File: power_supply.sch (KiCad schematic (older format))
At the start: 0 parts

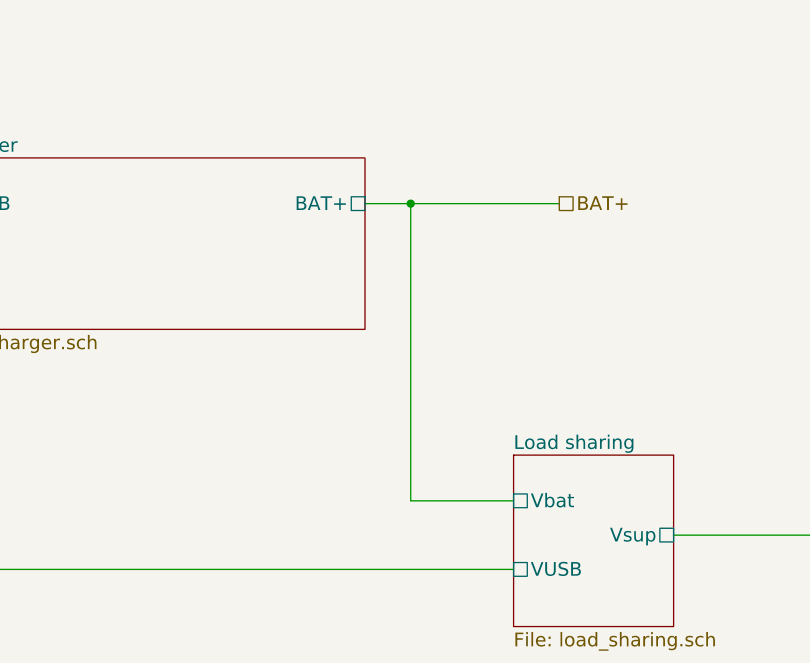
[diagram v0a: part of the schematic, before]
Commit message: Fixed NTLJF3117P MOSFET pin layout
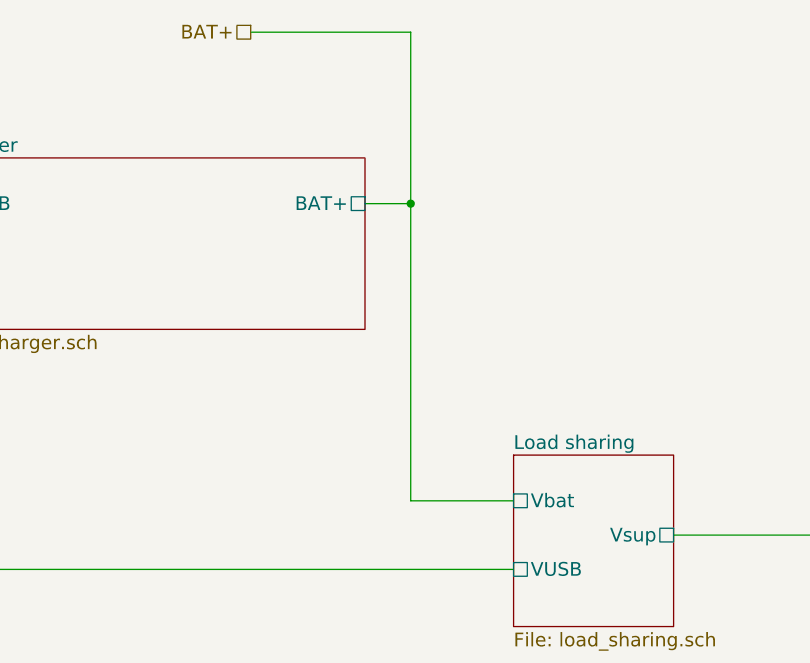
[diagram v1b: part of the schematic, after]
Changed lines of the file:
@@
 Text HLabel 1400 2900 0    60   UnSpc ~ 0
 VUSB
-Text HLabel 4800 2900 2    60   UnSpc ~ 0
+Text HLabel 3450 2150 0    60   UnSpc ~ 0
 BAT+
 $Sheet
@@
 $EndSheet
 Wire Wire Line
-	3950 2900 4800 2900
+	3950 2900 4150 2900
+Wire Wire Line
+	4150 2150 4150 4200
 Wire Wire Line
 	1400 2900 2100 2900
-Wire Wire Line
-	4150 2900 4150 4200
 Wire Wire Line
 	4150 4200 4600 4200
@@
 Wire Wire Line
 	8450 4400 7900 4400
+Wire Wire Line
+	3450 2150 4150 2150
 $EndSCHEMATC

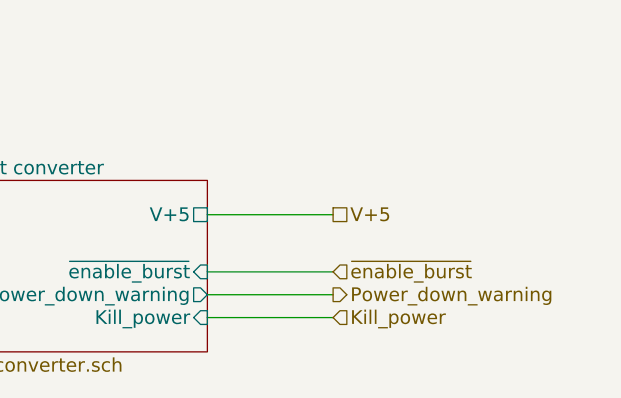
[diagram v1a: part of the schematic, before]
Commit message: Moved MCU pins around to make sure that they do not interfere with the programmer Moved ISP Header closer to the edge of the board to allow easier access with the programmer Added pulldown resistor to the DCD/DC converters enable pin to make sure it stays off in case of failure Added more PDFs of components
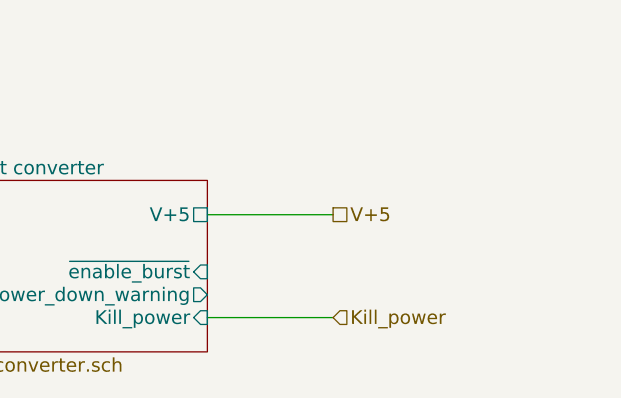
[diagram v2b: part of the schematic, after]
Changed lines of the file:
@@
 Wire Wire Line
 	8450 4600 7900 4600
-Text HLabel 8450 4500 2    60   Output ~ 0
-Power_down_warning
-Wire Wire Line
-	8450 4500 7900 4500
-Text HLabel 8450 4400 2    60   Input ~ 0
-~enable_burst
-Wire Wire Line
-	8450 4400 7900 4400
 Wire Wire Line
 	3450 2150 4150 2150

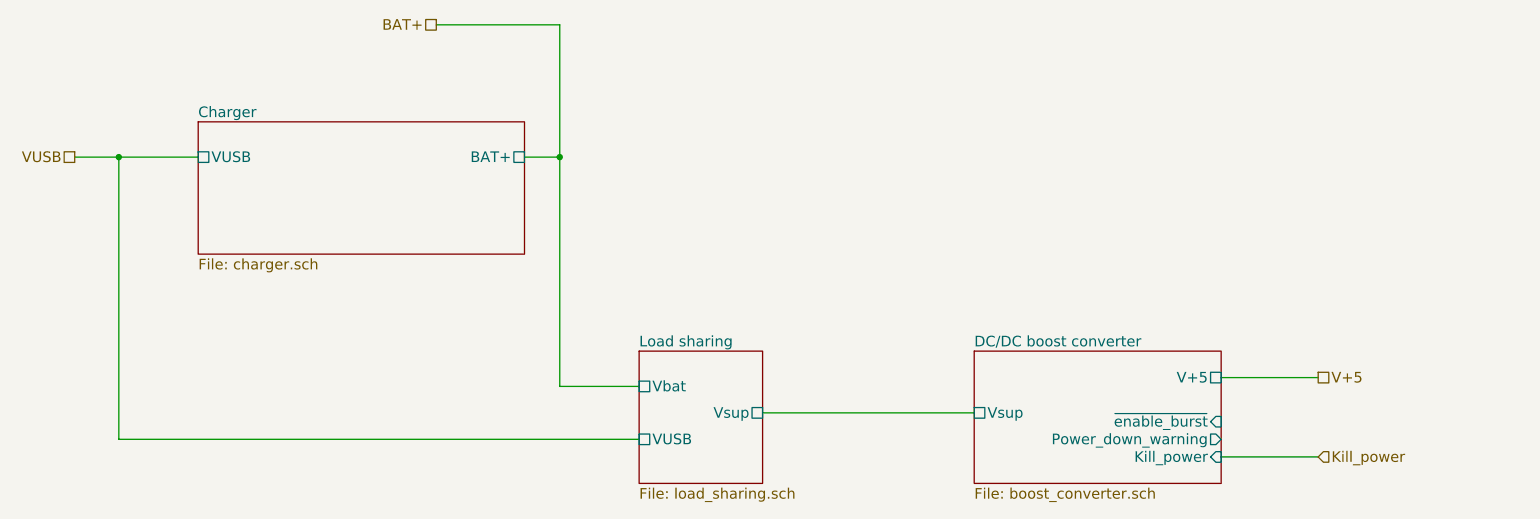
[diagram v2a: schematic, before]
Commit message: Preparing for v1.2 Updated to KiCAD 5 nightly Added resistors to isolate the programming pins Added transistor to drive the LED Replaced LTC3458 boost converter with an LTC3536 buck-boost converter to step down the USB power supply Added debugging jumper to test the voltage regulator
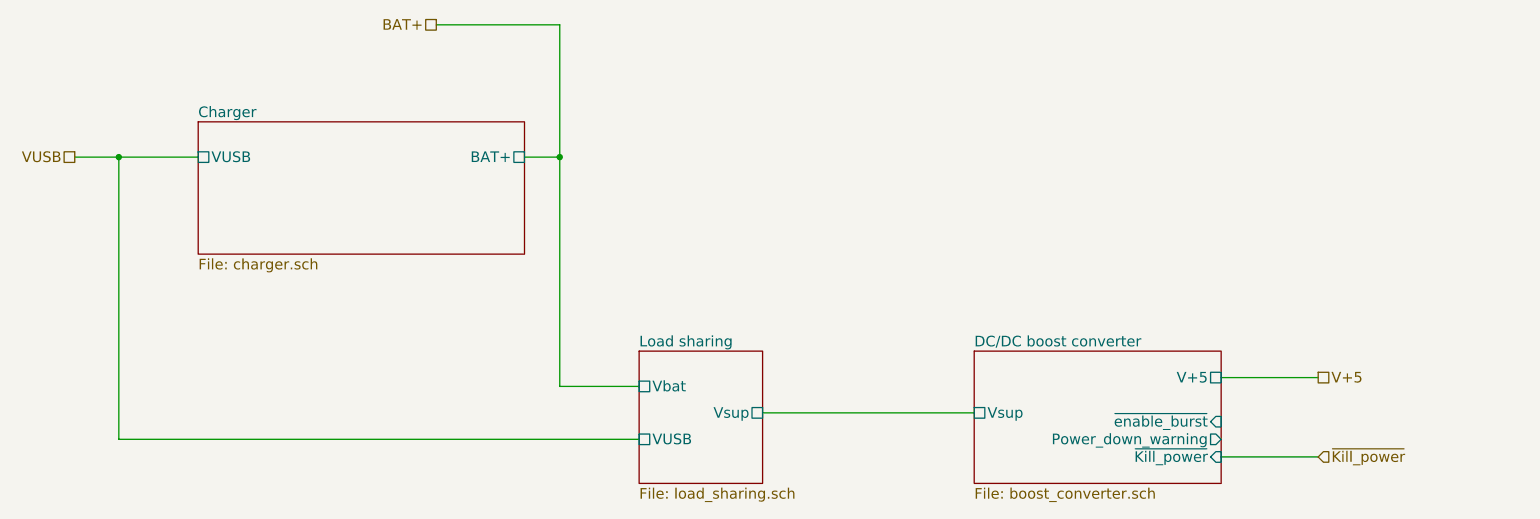
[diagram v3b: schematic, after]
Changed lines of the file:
@@
-EESchema Schematic File Version 2
-LIBS:power
-LIBS:device
-LIBS:transistors
-LIBS:conn
-LIBS:linear
-LIBS:regul
-LIBS:74xx
-LIBS:cmos4000
-LIBS:adc-dac
-LIBS:memory
-LIBS:xilinx
-LIBS:microcontrollers
-LIBS:dsp
-LIBS:microchip
-LIBS:analog_switches
-LIBS:motorola
-LIBS:texas
-LIBS:intel
-LIBS:audio
-LIBS:interface
-LIBS:digital-audio
-LIBS:philips
-LIBS:display
-LIBS:cypress
-LIBS:siliconi
-LIBS:opto
-LIBS:atmel
-LIBS:contrib
-LIBS:valves
-LIBS:switches
-LIBS:Microchip
-LIBS:On Semiconductor
-LIBS:Linear Technology
+EESchema Schematic File Version 4
 LIBS:main-cache
 EELAYER 26 0
@@
 	3950 2900 4150 2900
 Wire Wire Line
-	4150 2150 4150 4200
+	4150 2150 4150 2900
 Wire Wire Line
-	1400 2900 2100 2900
+	1400 2900 1650 2900
 Wire Wire Line
 	4150 4200 4600 4200
@@
 F3 "V+5" U R 7900 4150 60
 F4 "Power_down_warning" O R 7900 4500 60
-F5 "Kill_power" I R 7900 4600 60
+F5 "~Kill_power" I R 7900 4600 60
 F6 "~enable_burst" I R 7900 4400 60
 $EndSheet
@@
 	7900 4150 8450 4150
 Text HLabel 8450 4600 2    60   Input ~ 0
-Kill_power
+~Kill_power
 Wire Wire Line
 	8450 4600 7900 4600
 Wire Wire Line
 	3450 2150 4150 2150
+Wire Wire Line
+	4150 2900 4150 4200
+Wire Wire Line
+	1650 2900 2100 2900
 $EndSCHEMATC

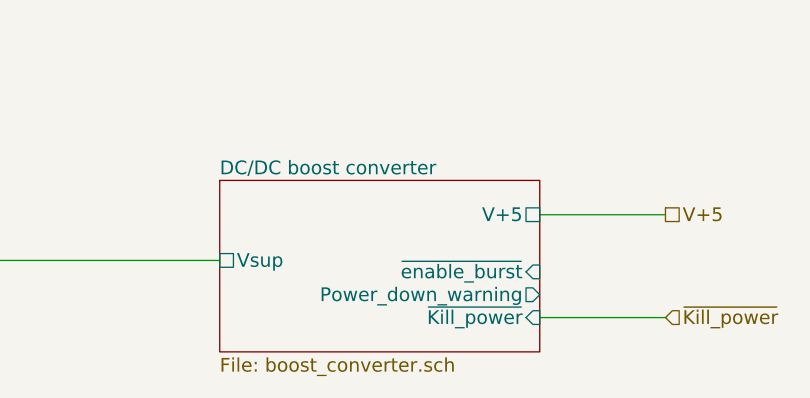
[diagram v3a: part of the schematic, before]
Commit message: Added power on state LED Updated to KiCAD 5.0
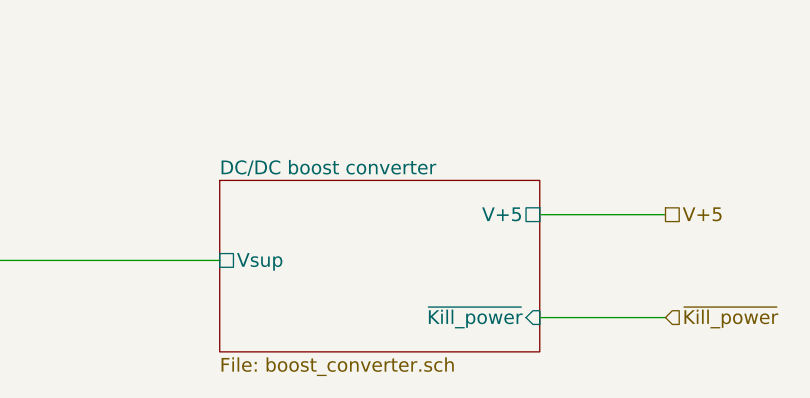
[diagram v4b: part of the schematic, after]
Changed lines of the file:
@@
 F2 "Vsup" U L 6500 4350 60
 F3 "V+5" U R 7900 4150 60
-F4 "Power_down_warning" O R 7900 4500 60
-F5 "~Kill_power" I R 7900 4600 60
-F6 "~enable_burst" I R 7900 4400 60
+F4 "~Kill_power" I R 7900 4600 60
 $EndSheet
 Wire Wire Line
